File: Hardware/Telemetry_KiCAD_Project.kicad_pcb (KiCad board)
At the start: 4 copper layers, 80 x 87.3 mm, 68 parts, among them J1 TX SPI Debug, J2 RX SPI Debug, J3 50Ω SMA Connector, J4 10118192-0001LF, J5 DB37_Male_MountingHoles, U1 STM32L562VET, U2 Si4463, U3 Si4463, U4 ADL5521, U5 RSD-897.500-942.500-1612-TR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

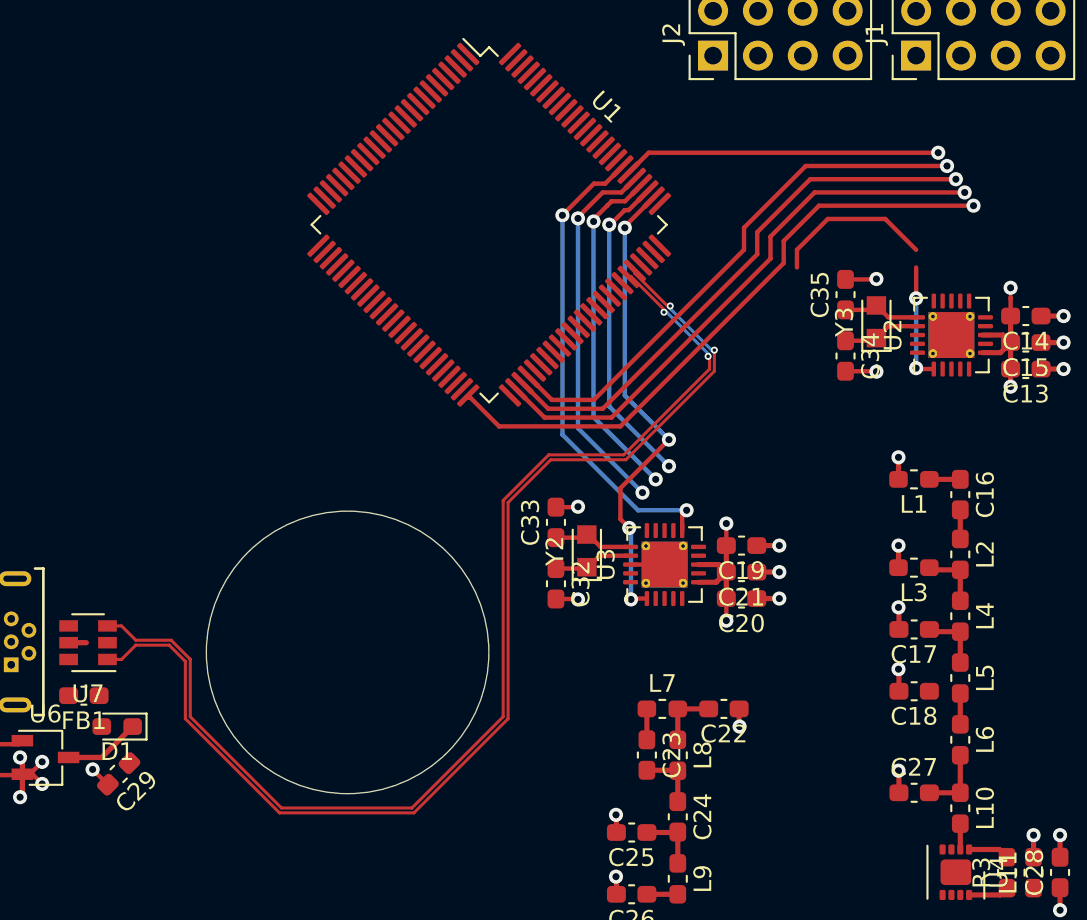
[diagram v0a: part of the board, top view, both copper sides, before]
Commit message: Routed TX Chip SPI bus
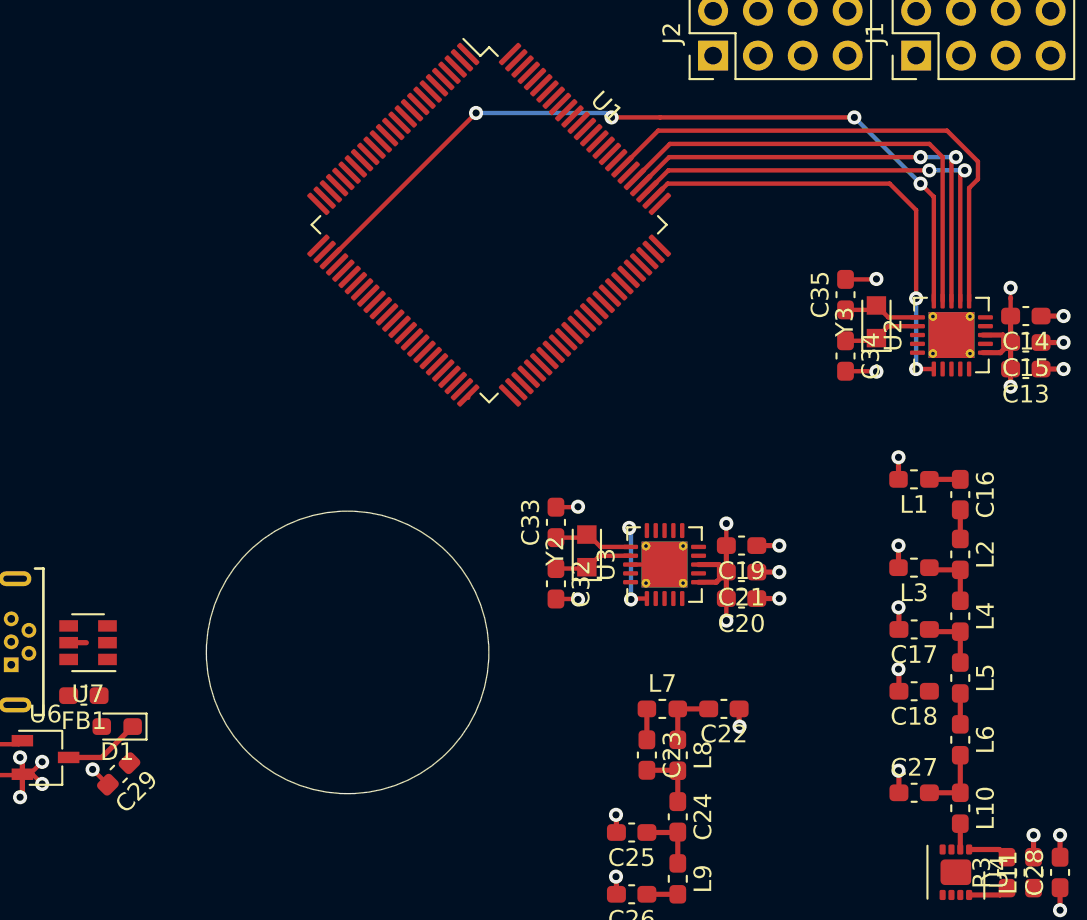
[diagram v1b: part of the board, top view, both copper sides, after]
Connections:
- U1 pad 28: /~RX_SEL -> /~TX_SEL
- U1 pad 50: /~TX_IRQ -> /~RX_IRQ
- U1 pad 52: /TX_SCL -> /RX_SCL
- U1 pad 53: /TX_SDO -> /RX_SDO
- U1 pad 54: /TX_SDI -> /RX_SDI
- U1 pad 55: /TX_RST -> /RX_RST
- U1 pad 77: /RX_RST -> /TX_RST
- U1 pad 78: /RX_SCL -> /TX_SCL
- U1 pad 79: /RX_SDO -> /TX_SDO
- U1 pad 80: /RX_SDI -> /TX_SDI
- U1 pad 81: /~TX_SEL -> /~RX_SEL
- U1 pad 82: /~RX_IRQ -> /~TX_IRQ
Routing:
- net /USB Connector and ESD/D+: track 65.8 -> 0.00 mm, vias 2 -> 0
- net /USB Connector and ESD/D-: track 65.2 -> 0.11 mm, vias 2 -> 0
- net /~TX_SEL: track 18.0 -> 45.4 mm, vias 1 -> 4
- net /~RX_IRQ: track 27.0 -> 0.13 mm, vias 2 -> 0
- net /RX_RST: track 27.0 -> 5.22 mm, vias 4 -> 2
- net /RX_SDI: track 21.2 -> 0.00 mm, vias 2 -> 0
- net /RX_SDO: track 19.7 -> 0.00 mm, vias 2 -> 0
- net /RX_SCL: track 18.0 -> 0.04 mm, vias 2 -> 0
- net /TX_RST: track 15.9 -> 25.8 mm
- net /TX_SCL: track 32.1 -> 26.0 mm, vias 1 -> 2
- net /~TX_IRQ: track 35.4 -> 29.8 mm, vias 1 -> 0
- net /TX_SDO: track 31.3 -> 26.7 mm, vias 1 -> 2
- net /TX_SDI: track 30.5 -> 26.7 mm, vias 1 -> 0

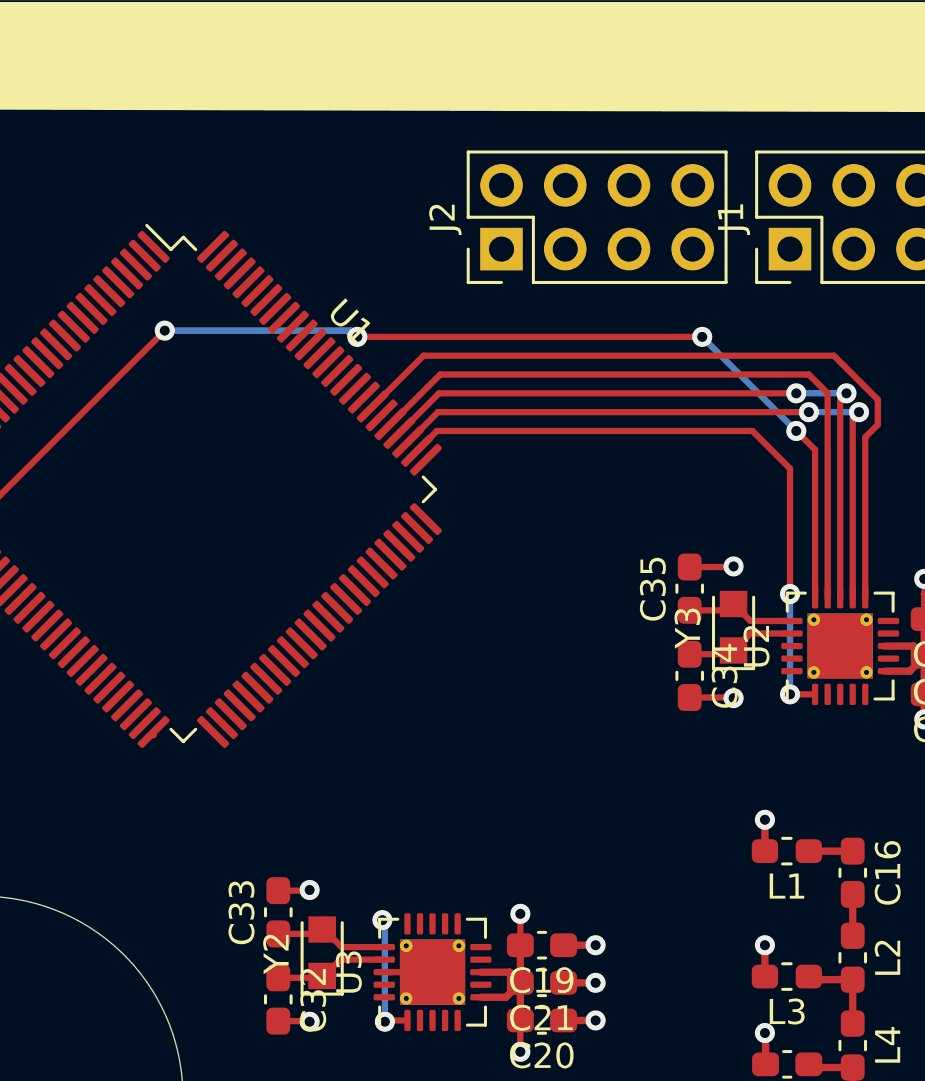
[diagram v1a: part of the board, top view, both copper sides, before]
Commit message: Routed RX Chip SPI bus
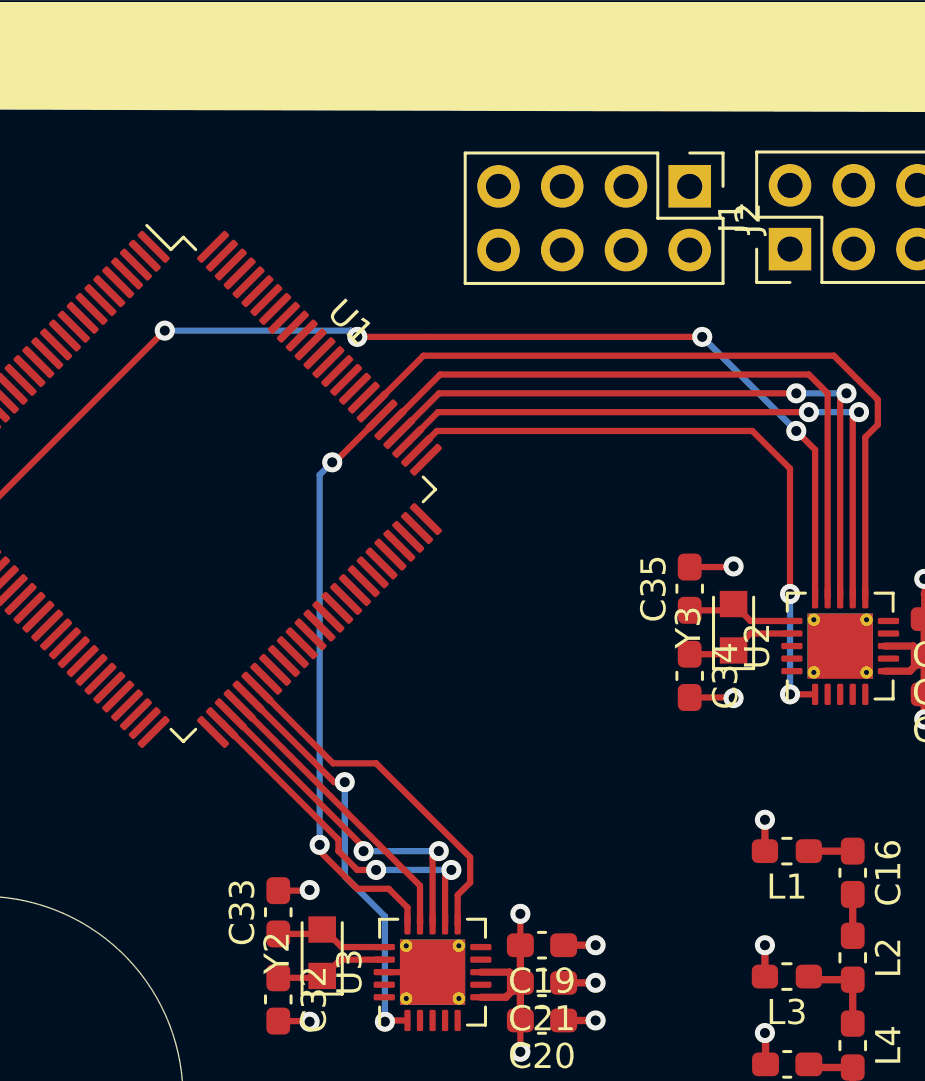
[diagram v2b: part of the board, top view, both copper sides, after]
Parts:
- moved J2 7.91 mm to (171.5, 62.8), turned to 270 degrees
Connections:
- U1 pad 50: /~RX_IRQ -> Net-(U1-Pad50)
- U1 pad 56: Net-(U1-Pad56) -> /~RX_IRQ
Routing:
- net /~RX_SEL: track 0.00 -> 23.5 mm, vias 0 -> 2
- net /RX_SCL: track 0.04 -> 14.1 mm, vias 0 -> 2
- net /~RX_IRQ: track 0.13 -> 14.1 mm
- net /RX_SDO: track 0.00 -> 13.7 mm, vias 0 -> 2
- net /RX_SDI: track 0.00 -> 11.8 mm
- net /RX_RST: track 5.22 -> 16.6 mm

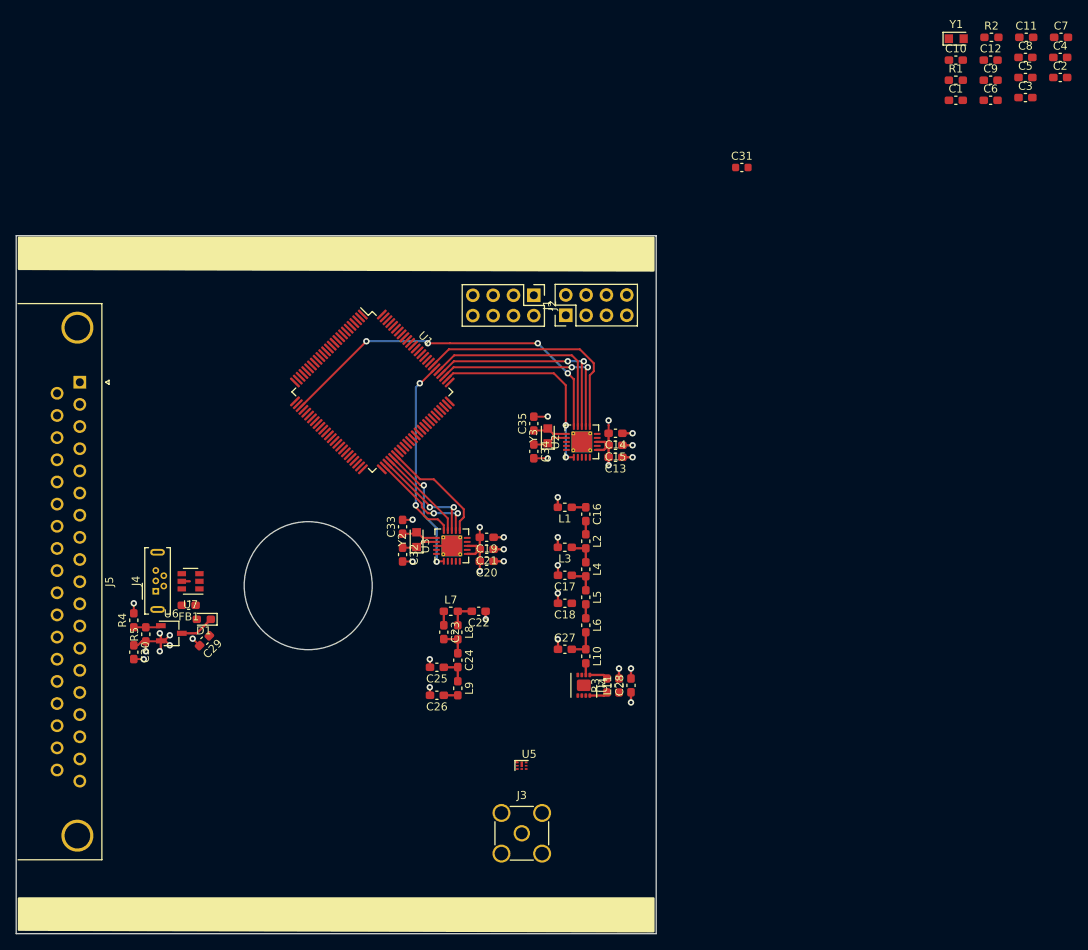
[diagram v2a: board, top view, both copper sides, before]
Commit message: Routed DB37 connector
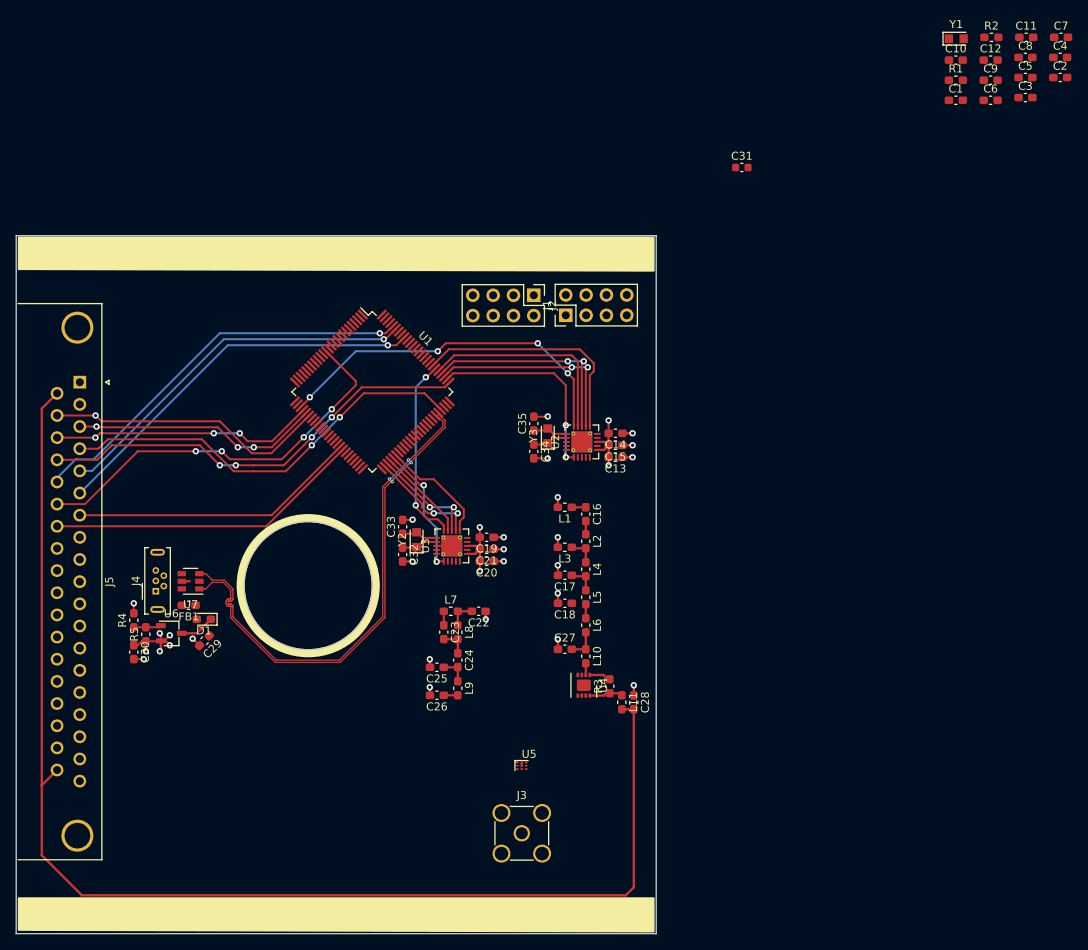
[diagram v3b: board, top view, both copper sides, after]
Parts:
- moved C28 2.15 mm to (184.0, 113.6), turned to 270 degrees
- moved L11 2.13 mm to (182.5, 113.6), turned to 270 degrees
- moved R3 0.36 mm to (181.0, 111.6)
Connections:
- U1 pad 42: Net-(U1-Pad42) -> /MCU_L562VE/ABORT_1
- U1 pad 43: Net-(U1-Pad43) -> /MCU_L562VE/ABORT_2
- U1 pad 68: /MCU_L562VE/ABORT_1 -> Net-(U1-Pad68)
- U1 pad 69: /MCU_L562VE/ABORT_2 -> Net-(U1-Pad69)
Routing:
- net +5V: track 7.85 -> 166.8 mm, vias 2 -> 0
- net /USB Connector and ESD/D+: track 0.00 -> 62.1 mm, vias 0 -> 2
- net /USB Connector and ESD/D-: track 0.11 -> 61.5 mm, vias 0 -> 2
- net /MCU_L562VE/DEBUG_SWCLK: track 0.00 -> 55.4 mm, vias 0 -> 4
- net /MCU_L562VE/DEBUG_SWDIO: track 0.00 -> 52.2 mm, vias 0 -> 2
- net /37 Pin DSUB/Alert_sda: track 0.00 -> 50.4 mm, vias 0 -> 1
- net /37 Pin DSUB/NRST: track 0.00 -> 50.4 mm, vias 0 -> 4
- net /37 Pin DSUB/Alert_Active: track 0.00 -> 48.6 mm, vias 0 -> 1
- net /37 Pin DSUB/Alert_scl: track 0.00 -> 46.9 mm, vias 0 -> 1
- net /MCU_L562VE/ABORT_2: track 0.00 -> 39.7 mm
- net /MCU_L562VE/ABORT_1: track 0.00 -> 36.1 mm
- net /MCU_L562VE/SPI1_MOSI: track 0.00 -> 35.4 mm, vias 0 -> 1
- net /MCU_L562VE/SPI1_SCK: track 0.00 -> 33.3 mm, vias 0 -> 3
- net /MCU_L562VE/SPI1_MISO: track 0.00 -> 31.2 mm, vias 0 -> 3
- net Net-(L11-Pad1): track 2.31 -> 3.91 mm

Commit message: Routed debug connectors
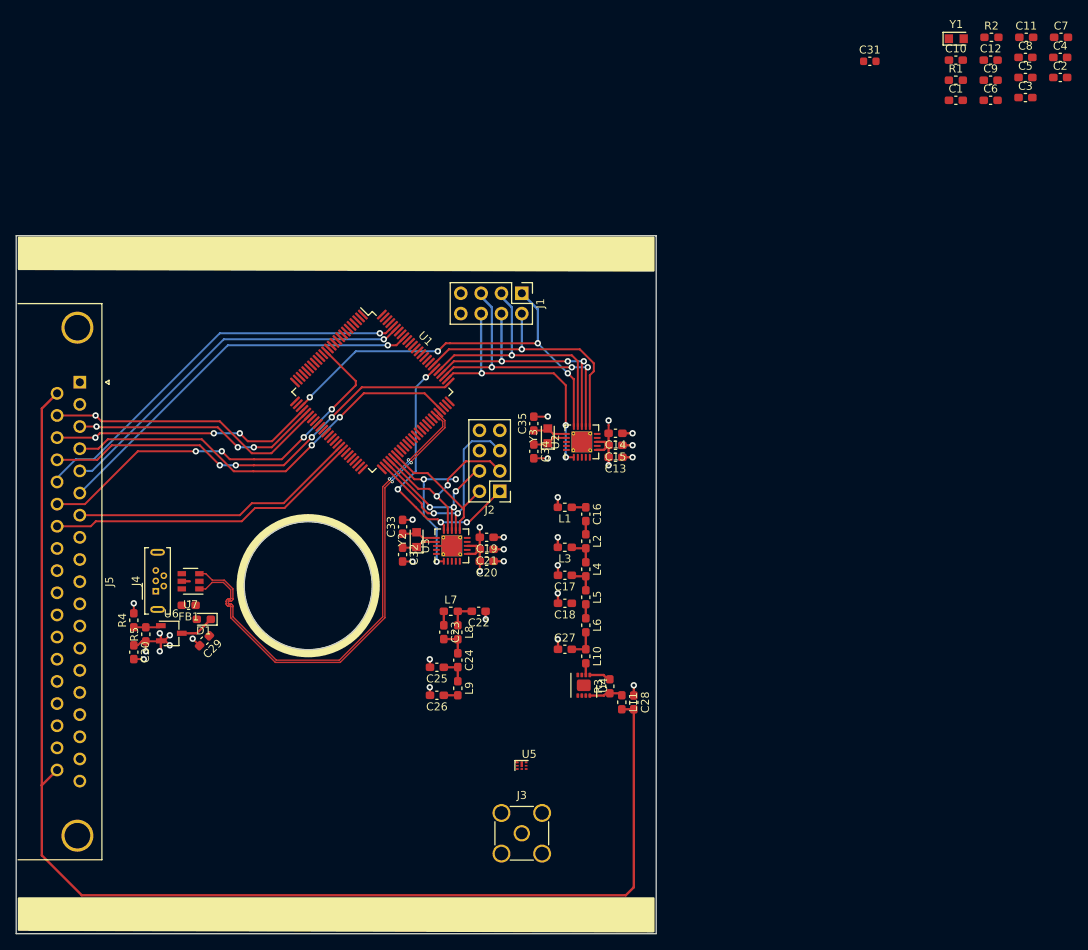
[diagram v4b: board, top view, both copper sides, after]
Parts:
- moved J2 24.9 mm to (167.2, 87.2), turned to 180 degrees
- moved C31 20.8 mm to (213.5, 33.5)
- moved J1 6.15 mm to (170.0, 62.5), turned to 270 degrees
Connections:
- J1 pad 1: /TX_RST -> /~TX_SEL
- J1 pad 2: /~TX_SEL -> /~TX_IRQ
- J1 pad 6: /~TX_IRQ -> /TX_RST
- J2 pad 1: /RX_RST -> /~RX_SEL
- J2 pad 2: /~RX_SEL -> /~RX_IRQ
- J2 pad 6: /~RX_IRQ -> /RX_RST
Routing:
- net /RX_SCL: track 14.1 -> 27.8 mm
- net /RX_SDI: track 11.8 -> 23.3 mm, vias 0 -> 2
- net /~RX_SEL: track 23.5 -> 34.6 mm, vias 2 -> 4
- net /TX_SCL: track 26.0 -> 35.8 mm, vias 2 -> 3
- net /TX_SDI: track 26.7 -> 35.0 mm, vias 0 -> 1
- net /TX_RST: track 25.8 -> 33.3 mm, vias 2 -> 3
- net /~TX_SEL: track 45.3 -> 52.3 mm
- net /RX_SDO: track 13.7 -> 19.8 mm, vias 2 -> 3
- net /TX_SDO: track 26.7 -> 32.7 mm, vias 2 -> 3
- net /RX_RST: track 16.6 -> 21.8 mm, vias 2 -> 3
- net /~TX_IRQ: track 29.8 -> 34.3 mm, vias 0 -> 1
- net /~RX_IRQ: track 14.1 -> 17.2 mm

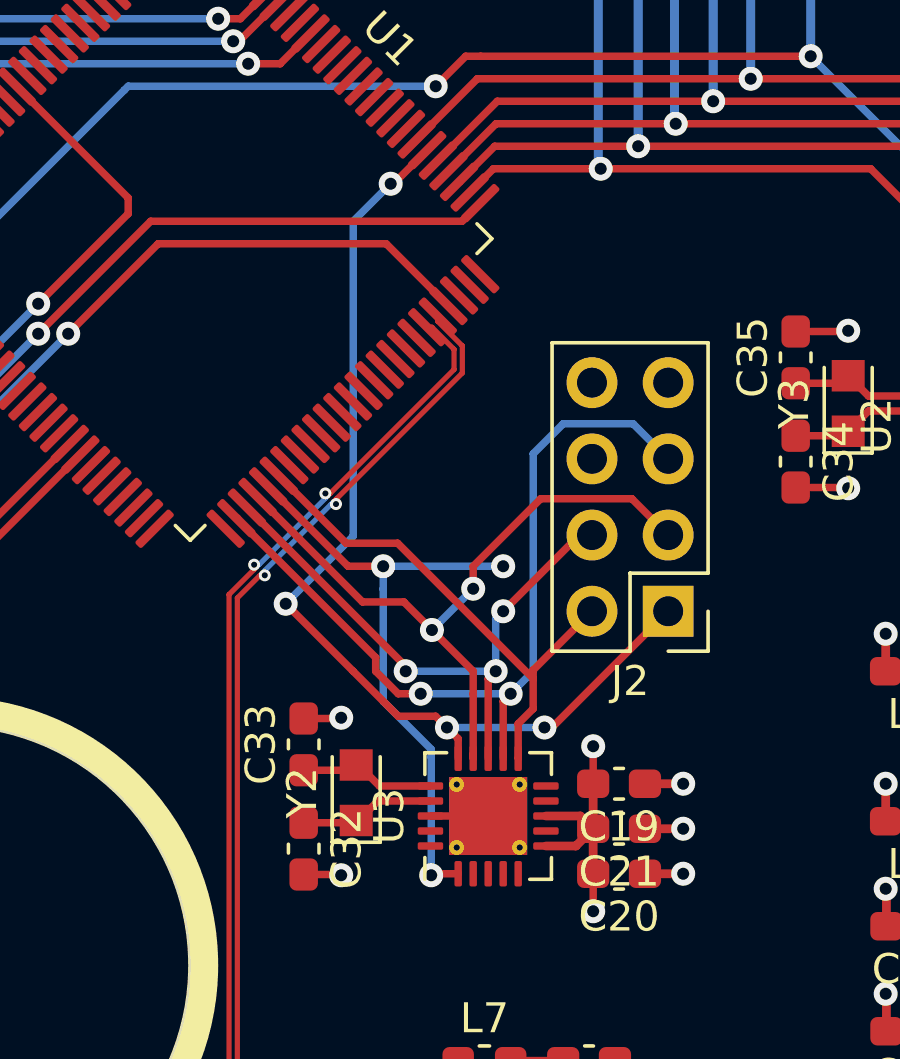
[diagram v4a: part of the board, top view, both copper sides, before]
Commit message: Reworked RX SPI lines
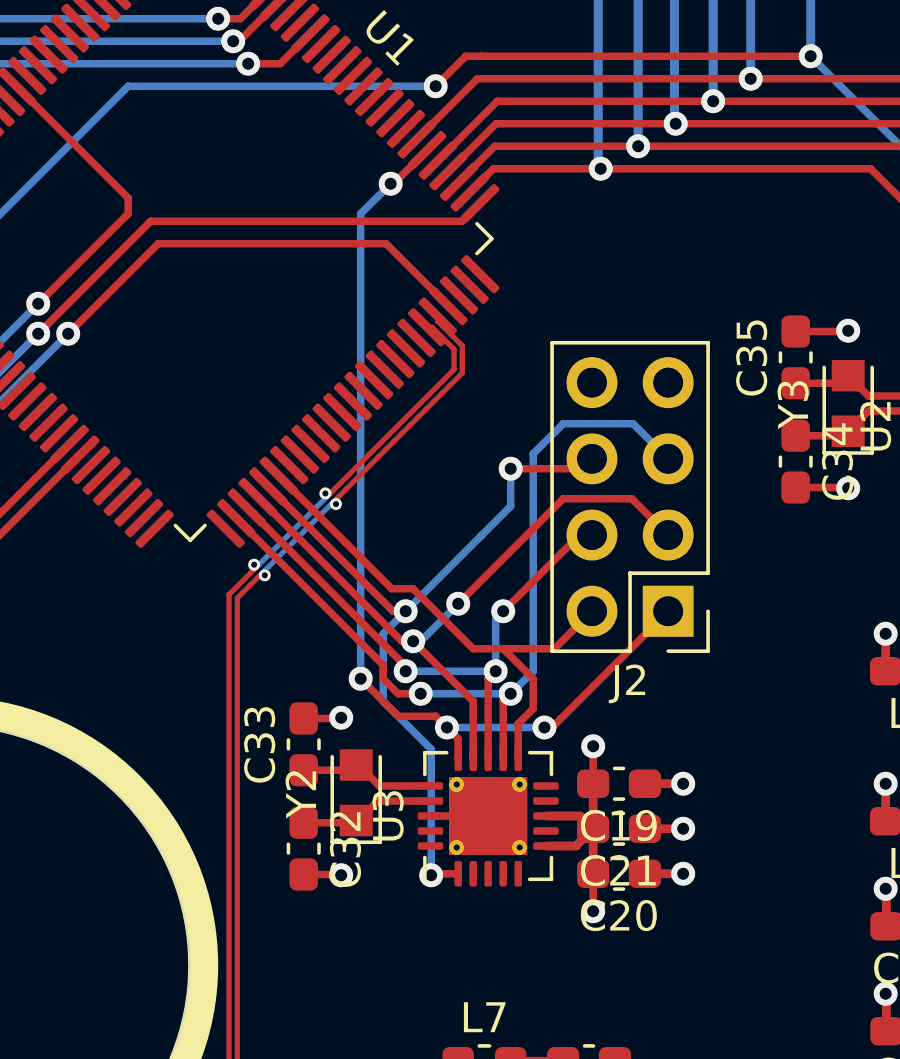
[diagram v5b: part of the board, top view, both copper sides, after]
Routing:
- net /RX_RST: track 21.8 -> 27.0 mm
- net /~RX_SEL: track 34.6 -> 32.6 mm
